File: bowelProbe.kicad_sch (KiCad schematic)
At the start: 100 parts, among them J1 Conn_01x01, J10 Conn_01x01, J11 Conn_02x03_Odd_Even, J12 Conn_01x01, J13 Conn_01x01, J14 Conn_01x01, J15 Conn_01x01, J16 Conn_01x01, J17 Conn_01x01, J18 Conn_01x01, J19 Conn_01x01, J2 Conn_01x01, J20 Conn_01x01, J21 Conn_01x01, J3 Conn_01x08, J4 Conn_01x08, J5 Conn_01x01, J6 Conn_01x01, J7 Conn_01x01, J8 Conn_01x01, J9 Conn_01x01, U10 TLV76050DBZR, U11 TL072ACDR, U2 LT8330, U3 ATmega328P, U4 AD9833BRMZ, U6 OPA2134UA/2K5, U7 TL072ACDR, U8 MCP6002T-E/MC, U9 LM3480IM3-12/NOPB

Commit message: Major Updates
Added architecture for phase detection which consists of 3 major stages: comparator stage, XOR stage, and low pass filter stage

Parts chosen and files downloaded and organized into corresponding folders

Simulation of updated circuit coming up soon (note LM311 simulation file used in place of LM319 due to no available file for LM319)

Added pull up resistors for I2C lines
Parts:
- added C28: 1u, BowelProbe:Cap1uF, symbol Device:C_Small
- added C49, C51, C54, C56: 0.1u, BowelProbe:Cap0.1uF, symbol Device:C_Small
- added C50, C52, C53, C55: 10u, BowelProbe:Cap10uF, symbol Device:C_Small
- added J22, J23, J24, J25: Conn_01x01, BowelProbe:CT3149-2, symbol Connector_Generic:Conn_01x01
- added R19, R20, R21, R22, R23: 10k, BowelProbe:Resistor10k, symbol Device:R_US
- added U1: LM319MX/NOPB, BowelProbe:LM319MX_NOPB, symbol BowelProbe:LM319MX/NOPB
- added U12: Buffer, BowelProbe:Buffer, symbol BowelProbe:Buffer
- added U5: SN74LVC1G86DBVR, BowelProbe:SN74LVC1G86DBVR, symbol BowelProbe:SN74LVC1G86DBVR
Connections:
- net +12V: now also C49.1, C50.1, U1.11 (V+)
- net +5V: now also C53.1, C54.1, C55.1, C56.1, R19.2, R20.1, R22.2, R23.2, U12.5 (V+), U5.5 (Vcc)
- net -12V: now also C51.2, C52.2, U1.6 (V-)
- net GND: now also C28.1, C49.2, C50.2, C51.1, C52.1, C53.2, C54.2, C55.2, C56.2, U1.10 (-IN2), U1.3 (GND1), U1.5 (-IN1), U1.8 (GND2), U12.2 (V-), U5.3 (GND)
- net SCL: now also R22.1
- net SDA: now also R23.1
- net Vampbuf: now also U1.4 (+IN1)
- net Vprobe: now also U1.9 (+IN2)
- net A6 renamed PDoutBuf
- net PDoutBuf: now also U12.3 (-IN), U12.4 (OUT)
- new net A: J23.1 (Pin_1), R19.1, U1.12 (OUT1), U5.1 (A)
- new net B: J22.1 (Pin_1), R20.2, U1.7 (OUT2), U5.2 (B)
- new net PDout: C28.2, J25.1 (Pin_1), R21.1, U12.1 (+IN)
- new net Y: J24.1 (Pin_1), R21.2, U5.4 (Y)
- no-connect marks 13 -> 16
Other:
- note added: "1. Magnitude 2. Phase"
- note added: "Magnitude"
- note added: "Now diverges into two signal paths:"
- note added: "Phase"
- note added: "Phase Detector & Buffering"
- note added: "Zero Cross Comparators"
- moved on the sheet: C1, C10, C11, C12, C13, C14, C15, C16, C17, C18, C19, C2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

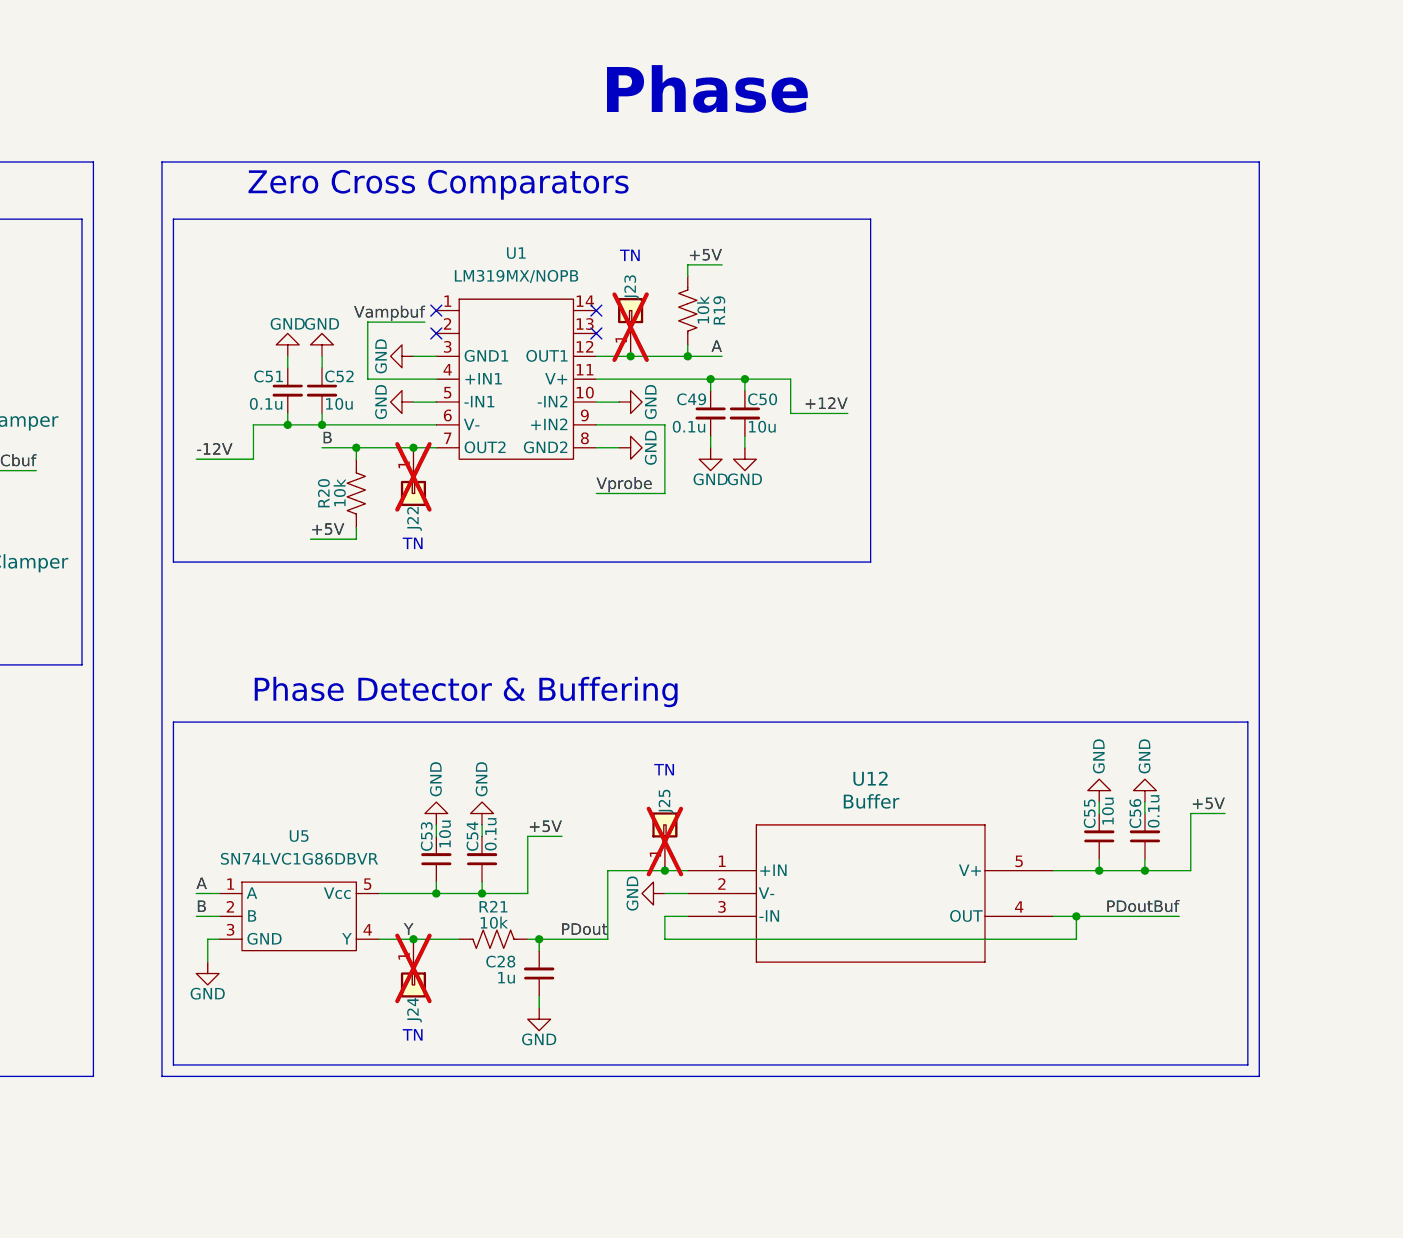
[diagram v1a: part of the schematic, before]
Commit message: Schematic Change
Very minor change: adjusted phase detector low pass stage to be second order low pass with 30k resistors and 0.1 uF capacitors.
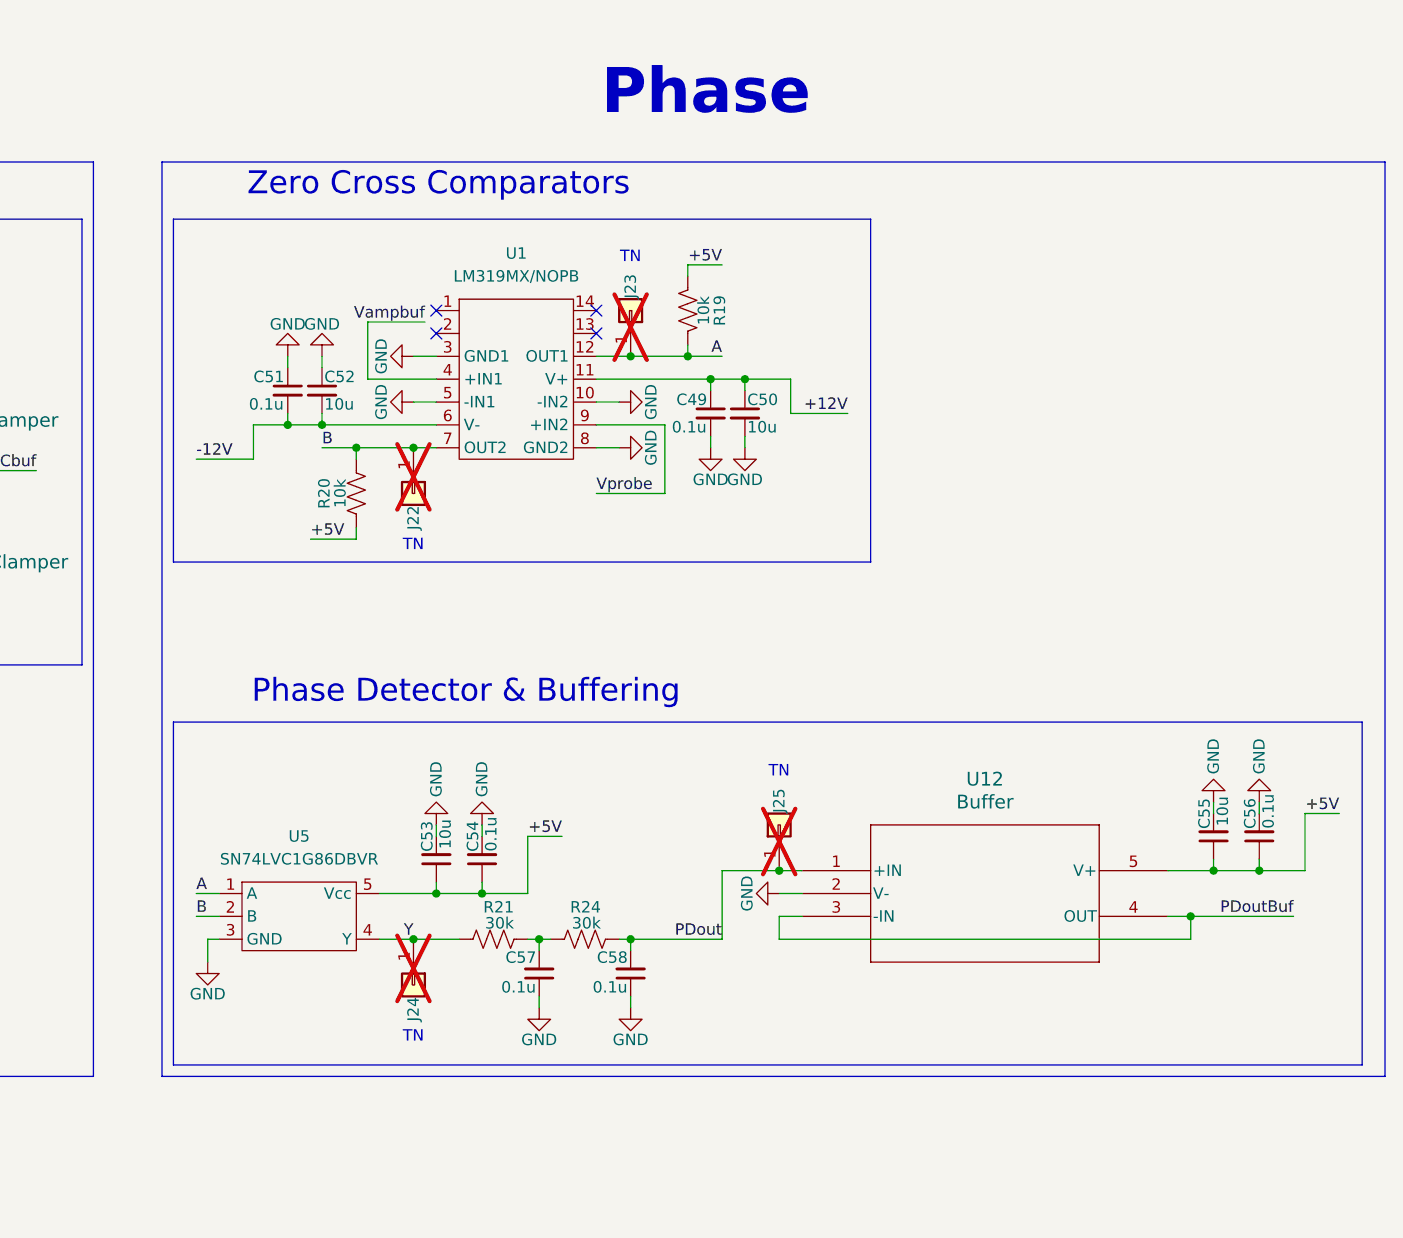
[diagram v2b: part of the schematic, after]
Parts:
- removed C28: 1u, BowelProbe:Cap1uF, symbol Device:C_Small
- added C57, C58: 0.1u, BowelProbe:Cap0.1uF, symbol Device:C_Small
- added R24: 30k, BowelProbe:Resistor30k, symbol Device:R_US
- R21: value 10k -> 30k; footprint BowelProbe:Resistor10k -> BowelProbe:Resistor30k; LCSC PN C98220 -> C137314; Manufacturer Product Number RC0603FR-0710KL -> RC1206FR-0730KL
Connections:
- net GND: now also C57.1, C58.1
- net PDout: now also C58.2, R24.2; no longer R21.1
- net Y: now also R21.1; no longer R21.2
- new net: C57.2, R21.2, R24.1
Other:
- moved on the sheet: C55, C56, J25, U12

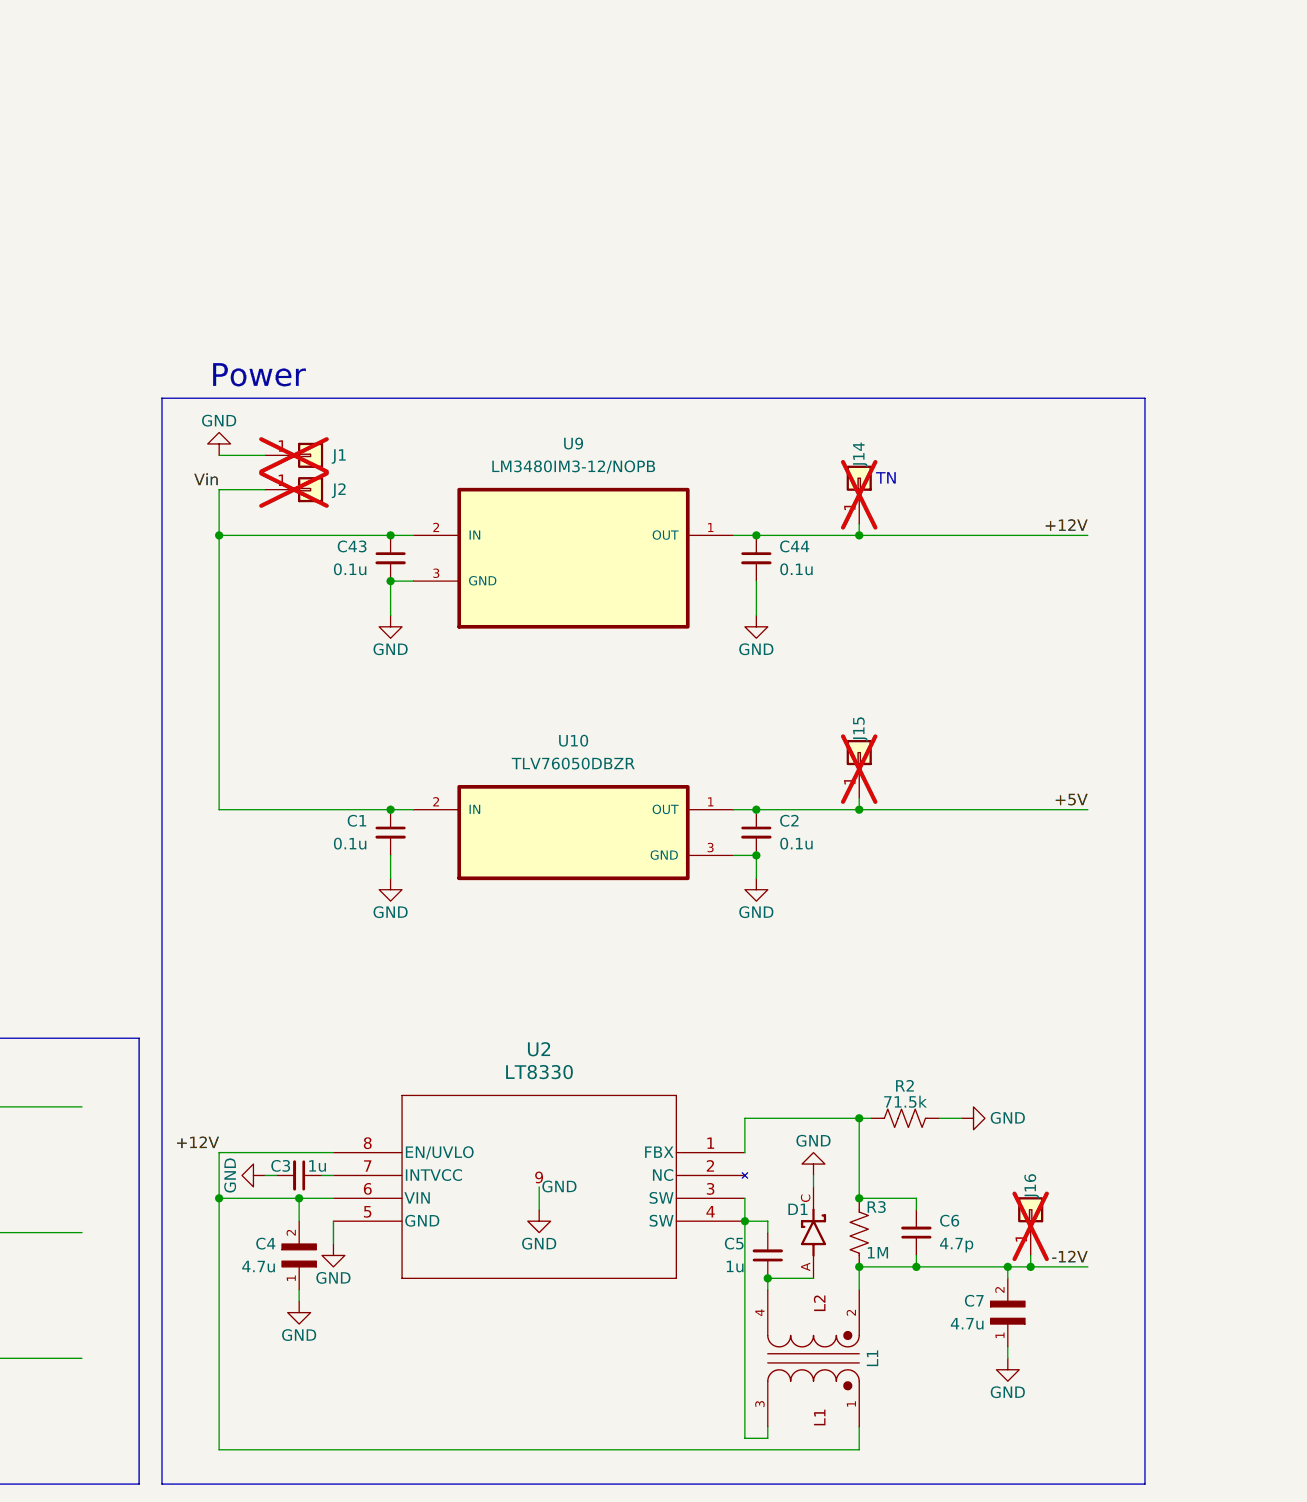
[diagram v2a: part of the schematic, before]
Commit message: Final Major Schematic Architecture Updates (Rev 1)
Added architecture for reverse polarity protection. Added parts files necessary for this circuit and organized to the proper folders. Created spice files for PMOS and zener diode parts in reverse polarity protection circuit.
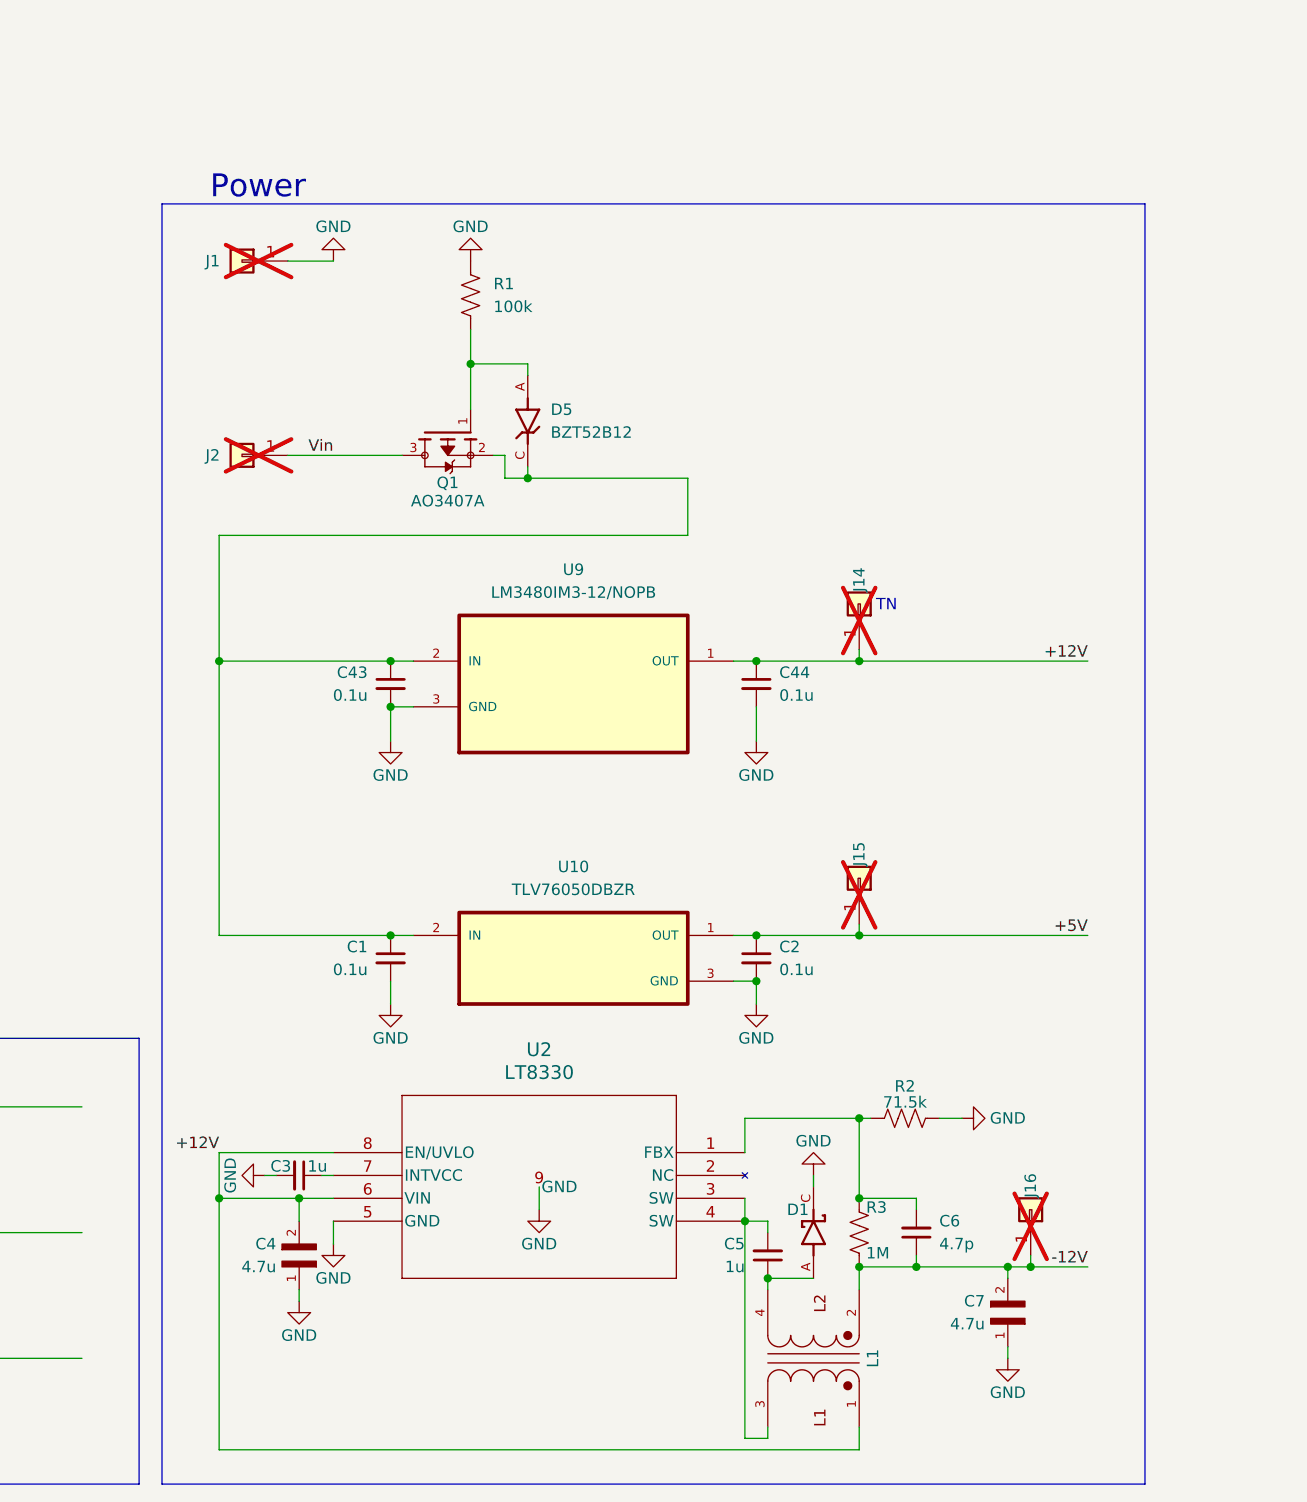
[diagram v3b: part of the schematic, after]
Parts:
- added D5: BZT52B12, BowelProbe:BZT52B12, symbol BowelProbe:BZT52B12
- added Q1: AO3407A, BowelProbe:AO3407A, symbol BowelProbe:AO3407A
- added R1: 100k, BowelProbe:Resistor100k, symbol Device:R_US
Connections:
- net GND: now also R1.1
- net Vin: now also Q1.3; no longer C1.1, C43.1, U10.2 (IN), U9.2 (IN)
- new net: D5.A, Q1.1, R1.2
- new net: C1.1, C43.1, D5.C, Q1.2, U10.2 (IN), U9.2 (IN)
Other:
- moved on the sheet: C1, C2, C43, C44, J1, J14, J15, J2, U10, U9
